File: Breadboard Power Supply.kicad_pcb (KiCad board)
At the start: 2 copper layers, 29 x 52.6 mm, 18 parts, among them J1 Barrel_Jack_Switch, J2 Conn_01x03_Male, J3 Conn_01x02_Male, J4 Screw_Terminal_01x02, J5 Conn_01x03_Male, J6 Conn_01x02_Male, J7 Screw_Terminal_01x02, U1 LM317_TO-220, U2 LM7805_TO220

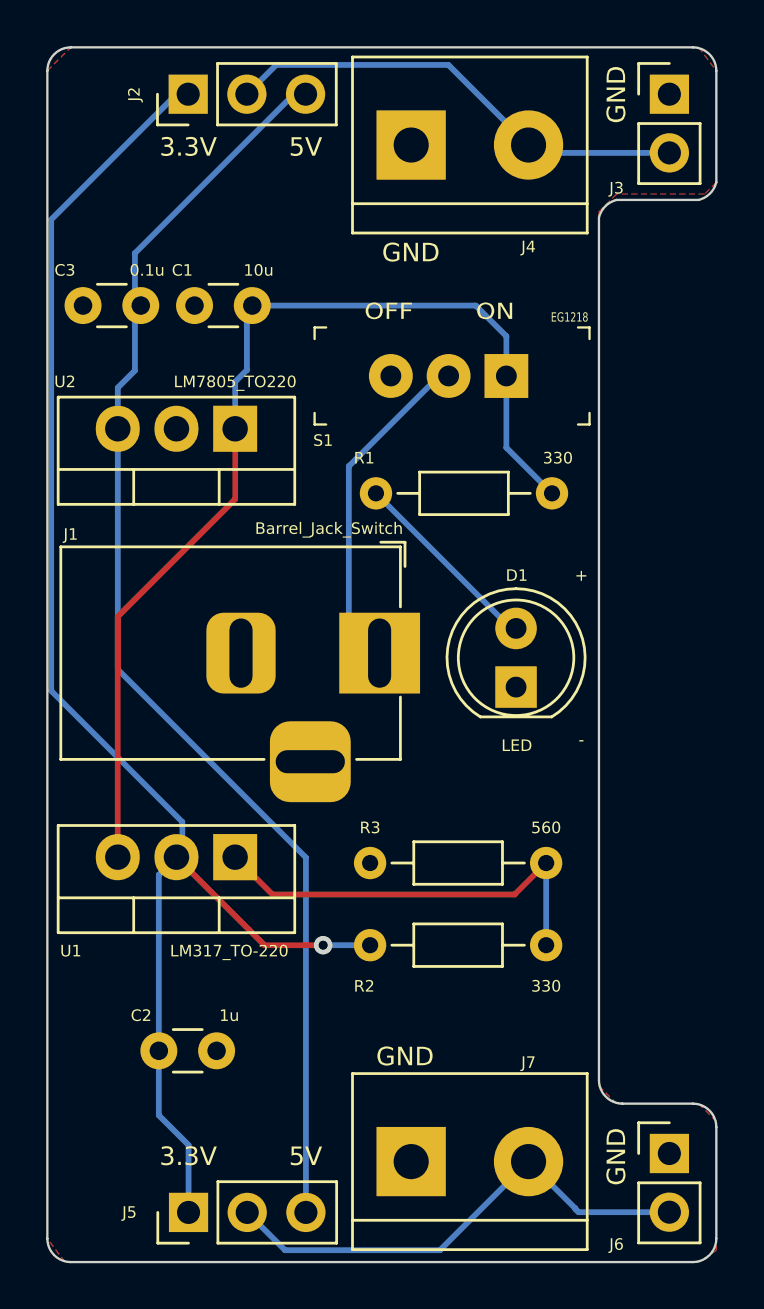
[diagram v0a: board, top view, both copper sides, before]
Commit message: reversed tracks for through hole plated version
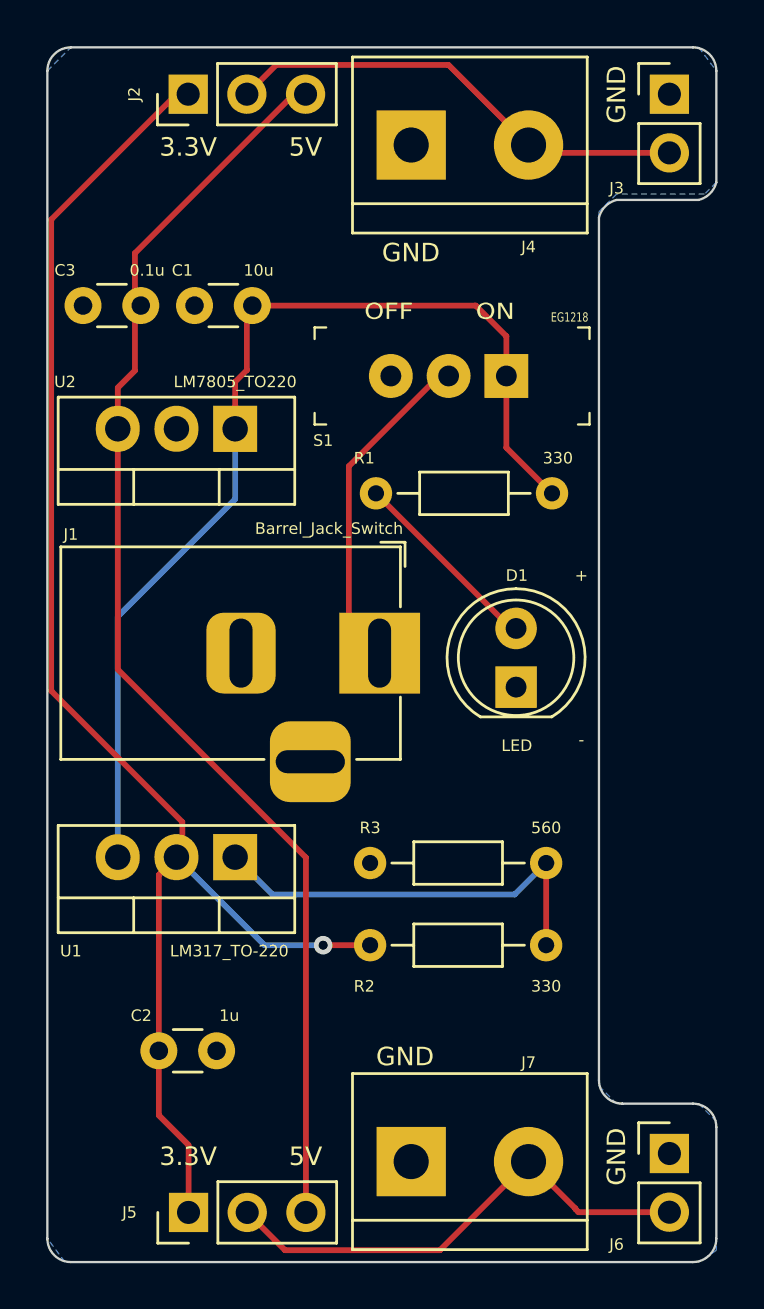
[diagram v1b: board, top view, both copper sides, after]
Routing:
- added copper zone on B.Cu, net GND
- removed copper zone on F.Cu, net GND
